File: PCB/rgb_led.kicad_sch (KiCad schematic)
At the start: 3 parts

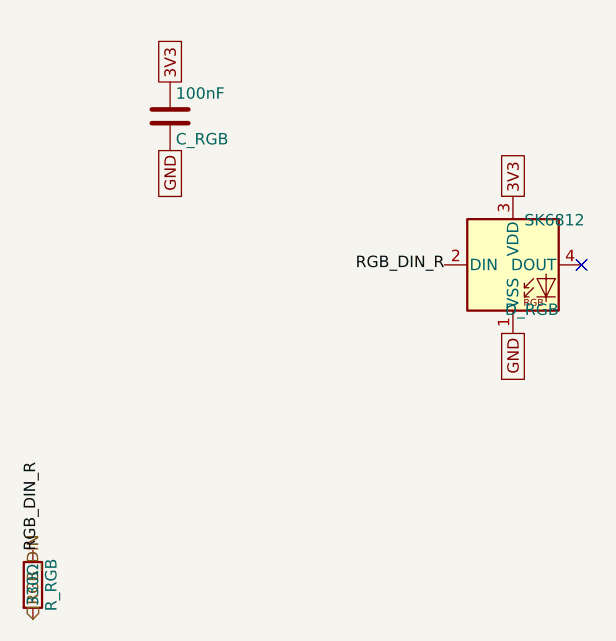
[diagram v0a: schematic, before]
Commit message: refactor: erc is clean
This gets the schematic as clean as it can be.
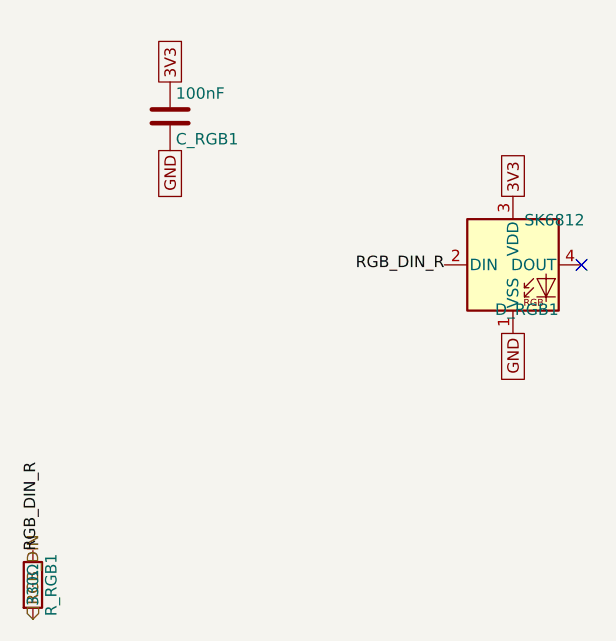
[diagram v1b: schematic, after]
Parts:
- removed C_RGB: 100nF, symbol Device:C
- removed D_RGB: SK6812, LED_SMD:LED_SK6812_PLCC4_5.0x5.0mm_P3.2mm, symbol LED:SK6812
- removed R_RGB: 330Ω, symbol Device:R
- added C_RGB1: 100nF, symbol Device:C
- added D_RGB1: SK6812, LED_SMD:LED_SK6812_PLCC4_5.0x5.0mm_P3.2mm, symbol LED:SK6812
- added R_RGB1: 330Ω, symbol Device:R
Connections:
- net 3V3: now also C_RGB1.1, D_RGB1.3 (VDD)
- net GND: now also C_RGB1.2, D_RGB1.1 (VSS)
- net RGB_DIN: now also R_RGB1.2
- net RGB_DIN_R: now also D_RGB1.2 (DIN), R_RGB1.1
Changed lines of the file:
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@@
+	)
+	(label "RGB_DIN_R"
+		(at 121.92 127 90)
+		(effects
+			(font
+				(size 1.27 1.27)
+			)
+			(justify left)
+		)
 	)
 	(label "RGB_DIN_R"
@@
 		)
 	)
-	(label "RGB_DIN_R"
-		(at 121.92 127 90)
+	(global_label "3V3"
+		(shape passive)
+		(at 175.26 87.63 90)
+		(fields_autoplaced yes)
 		(effects
 			(font
@@
 			)
 			(justify left)
+		)
+		(property "Intersheetrefs" "${INTERSHEET_REFS}"
+			(at 175.26 87.63 0)
+			(effects
+				(font
+					(size 1.27 1.27)
+				)
+				(hide yes)
+			)
 		)
 	)
@@
 		(property "Intersheetrefs" "${INTERSHEET_REFS}"
 			(at 137.16 74.93 0)
-			(effects
-				(font
-					(size 1.27 1.27)
-				)
-				(hide yes)
-			)
-		)
-	)
-	(global_label "3V3"
-		(shape passive)
-		(at 175.26 87.63 90)
-		(fields_autoplaced yes)
-		(effects
-			(font
-				(size 1.27 1.27)
-			)
-			(justify left)
-		)
-		(property "Intersheetrefs" "${INTERSHEET_REFS}"
-			(at 175.26 87.63 0)
 			(effects
 				(font
@@
 		(dnp no)
 		(fields_autoplaced yes)
-		(property "Reference" "C_RGB"
+		(property "Reference" "C_RGB1"
 			(at 137.795 81.28 0)
 			(effects
@@
 		(instances
 			(project "snips_controller"
-				(path "/2289c08f-f540-4e27-86fd-a28b71d1d149/d370bfd7-92c0-4db2-8e41-752e909926d0"
-					(reference "C_RGB")
+				(path "/70589bdd-acbd-4920-8e78-aa58d10832b9/fa750337-dd8a-4963-aa5f-de1f036c9ce0"
+					(reference "C_RGB1")
+					(unit 1)
+				)
+			)
+		)
+	)
+	(symbol
+		(lib_id "Device:R")
+		(at 121.92 130.81 0)
+		(unit 1)
+		(exclude_from_sim no)
+		(in_bom yes)
+		(on_board yes)
+		(dnp no)
+		(fields_autoplaced yes)
+		(property "Reference" "R_RGB1"
+			(at 123.952 130.81 90)
+			(effects
+				(font
+					(size 1.27 1.27)
+				)
+			)
+		)
+		(property "Value" "330Ω"
+			(at 121.92 130.81 90)
+			(effects
+				(font
+					(size 1.27 1.27)
+				)
+			)
+		)
+		(property "Footprint" ""
+			(at 120.142 130.81 90)
+			(effects
+				(font
+					(size 1.27 1.27)
+				)
+				(hide yes)
+			)
+		)
+		(property "Datasheet" "~"
+			(at 121.92 130.81 0)
+			(effects
+				(font
+					(size 1.27 1.27)
+				)
+				(hide yes)
+			)
+		)
+		(property "Description" "Resistor"
+			(at 121.92 130.81 0)
+			(effects
+				(font
+					(size 1.27 1.27)
+				)
+				(hide yes)
+			)
+		)
+		(pin "1"
+		)
+		(pin "2"
+		)
+		(instances
+			(project "snips_controller"
+				(path "/70589bdd-acbd-4920-8e78-aa58d10832b9/fa750337-dd8a-4963-aa5f-de1f036c9ce0"
+					(reference "R_RGB1")
 					(unit 1)
 				)
@@
 		(dnp no)
 		(fields_autoplaced yes)
-		(property "Reference" "D_RGB"
+		(property "Reference" "D_RGB1"
 			(at 180.34 100.965 0)
 			(effects
@@
 		(instances
 			(project "snips_controller"
-				(path "/2289c08f-f540-4e27-86fd-a28b71d1d149/d370bfd7-92c0-4db2-8e41-752e909926d0"
-					(reference "D_RGB")
+				(path "/70589bdd-acbd-4920-8e78-aa58d10832b9/fa750337-dd8a-4963-aa5f-de1f036c9ce0"
+					(reference "D_RGB1")
 					(unit 1)
 				)
-			)
-		)
-	)
-	(symbol
-		(lib_id "Device:R")
-		(at 121.92 130.81 0)
-		(unit 1)
-		(exclude_from_sim no)
-		(in_bom yes)
-		(on_board yes)
-		(dnp no)
-		(fields_autoplaced yes)
-		(property "Reference" "R_RGB"
-			(at 123.952 130.81 90)
-			(effects
-				(font
-					(size 1.27 1.27)
-				)
-			)
-		)
-		(property "Value" "330Ω"
-			(at 121.92 130.81 90)
-			(effects
-				(font
-					(size 1.27 1.27)
-				)
-			)
-		)
-		(property "Footprint" ""
-			(at 120.142 130.81 90)
-			(effects
-				(font
-					(size 1.27 1.27)
-				)
-				(hide yes)
-			)
-		)
-		(property "Datasheet" "~"
-			(at 121.92 130.81 0)
-			(effects
-				(font
-					(size 1.27 1.27)
-				)
-				(hide yes)
-			)
-		)
-		(property "Description" "Resistor"
-			(at 121.92 130.81 0)
-			(effects
-				(font
-					(size 1.27 1.27)
-				)
-				(hide yes)
-			)
-		)
-		(pin "1"
-		)
-		(pin "2"
-		)
-		(instances
-			(project "snips_controller"
-				(path "/2289c08f-f540-4e27-86fd-a28b71d1d149/d370bfd7-92c0-4db2-8e41-752e909926d0"
-					(reference "R_RGB")
-					(unit 1)
-				)

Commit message: refactor: switch over to esp32-s3-wroom1 (#13)
This refactors to the esp32-s3 to avoid every problem we encountered with the raspberry pi options.
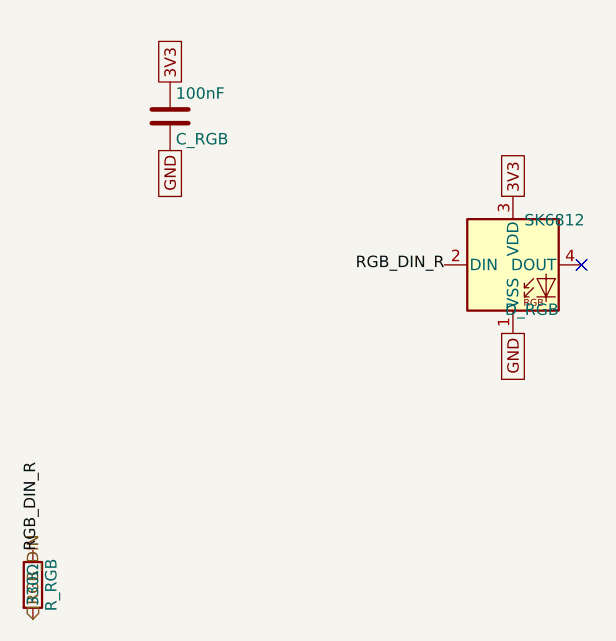
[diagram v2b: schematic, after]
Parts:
- removed C_RGB1: 100nF, symbol Device:C
- removed D_RGB1: SK6812, LED_SMD:LED_SK6812_PLCC4_5.0x5.0mm_P3.2mm, symbol LED:SK6812
- removed R_RGB1: 330Ω, symbol Device:R
- added C_RGB: 100nF, Capacitor_SMD:C_0402_1005Metric, symbol Device:C
- added D_RGB: SK6812, LED_SMD:LED_SK6812_PLCC4_5.0x5.0mm_P3.2mm, symbol LED:SK6812
- added R_RGB: 330Ω, Resistor_SMD:R_0402_1005Metric, symbol Device:R
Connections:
- net 3V3: now also C_RGB.1, D_RGB.3 (VDD)
- net GND: now also C_RGB.2, D_RGB.1 (VSS)
- net RGB_DIN: now also R_RGB.2
- net RGB_DIN_R: now also D_RGB.2 (DIN), R_RGB.1

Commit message: cleanup: annotations and library updates
This is just a task to update the kicad libraries and annotations internally to get that clean ERC.
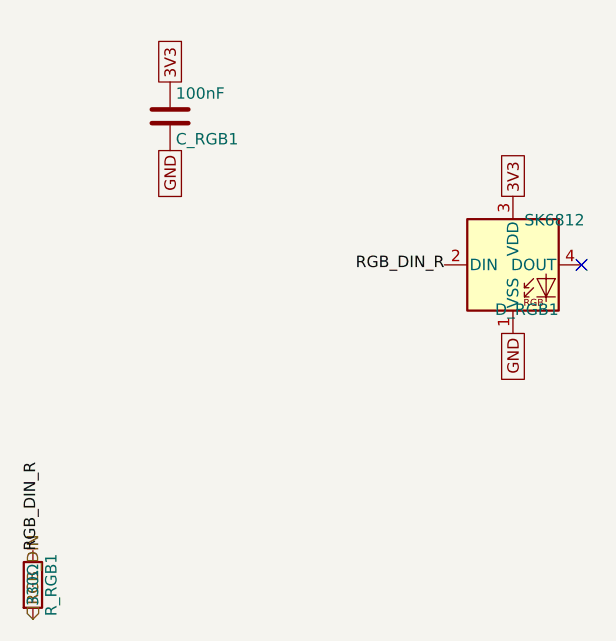
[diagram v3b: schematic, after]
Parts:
- renumbered C_RGB to C_RGB1, D_RGB to D_RGB1, R_RGB to R_RGB1
